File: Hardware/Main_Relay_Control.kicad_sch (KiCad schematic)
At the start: 10 parts, among them Q7 MJD41CT4G, U13 LTV-356T, U8 HF116F-80/24-1HTF

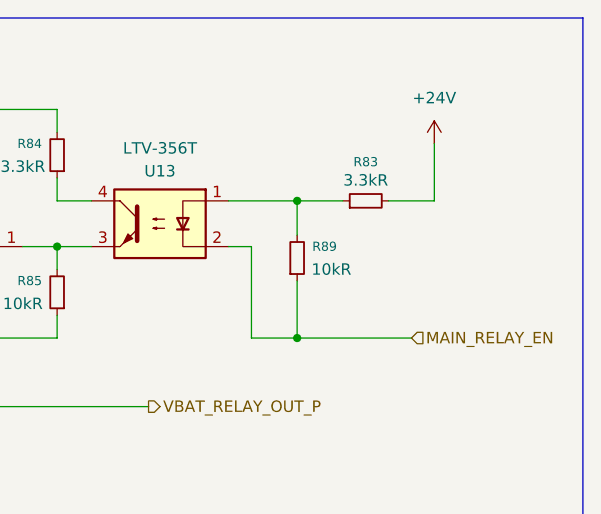
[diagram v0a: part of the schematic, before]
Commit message: fix(hardware): revise optocoupler control logic
Update relay and communication optocoupler drive networks, then synchronize the related PCB routing and KiCad project metadata.
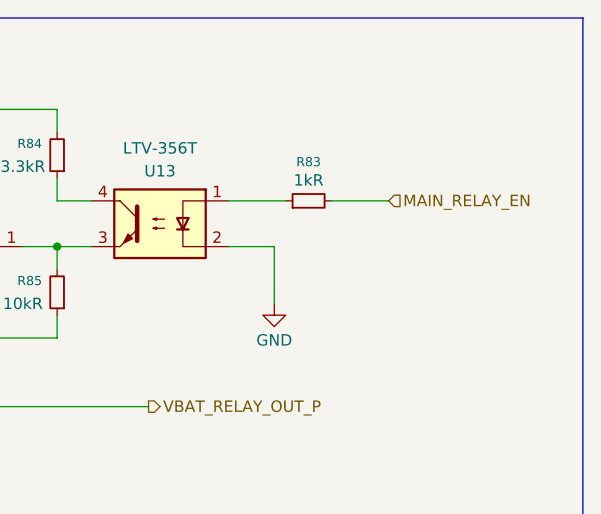
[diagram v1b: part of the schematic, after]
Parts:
- removed R89: 10kR, Resistor_SMD:R_0805_2012Metric, symbol Device:R_Small
- R83: value 3.3kR -> 1kR
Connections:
- net +24V: no longer R83.2
- net GND: now also U13.2
- net MAIN_RELAY_EN: now also R83.2; no longer U13.2
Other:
- moved on the sheet: R83
